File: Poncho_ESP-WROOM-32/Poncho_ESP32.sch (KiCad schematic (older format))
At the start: 20 parts, among them J1 JP_Vcc, J2 JP_TX, J3 JP_RX, J4 CONN_USB2UART, J5 BOOT OPTION, J6 JTAG, U1 LD1117AL-33, U2 ESP32-WROOM

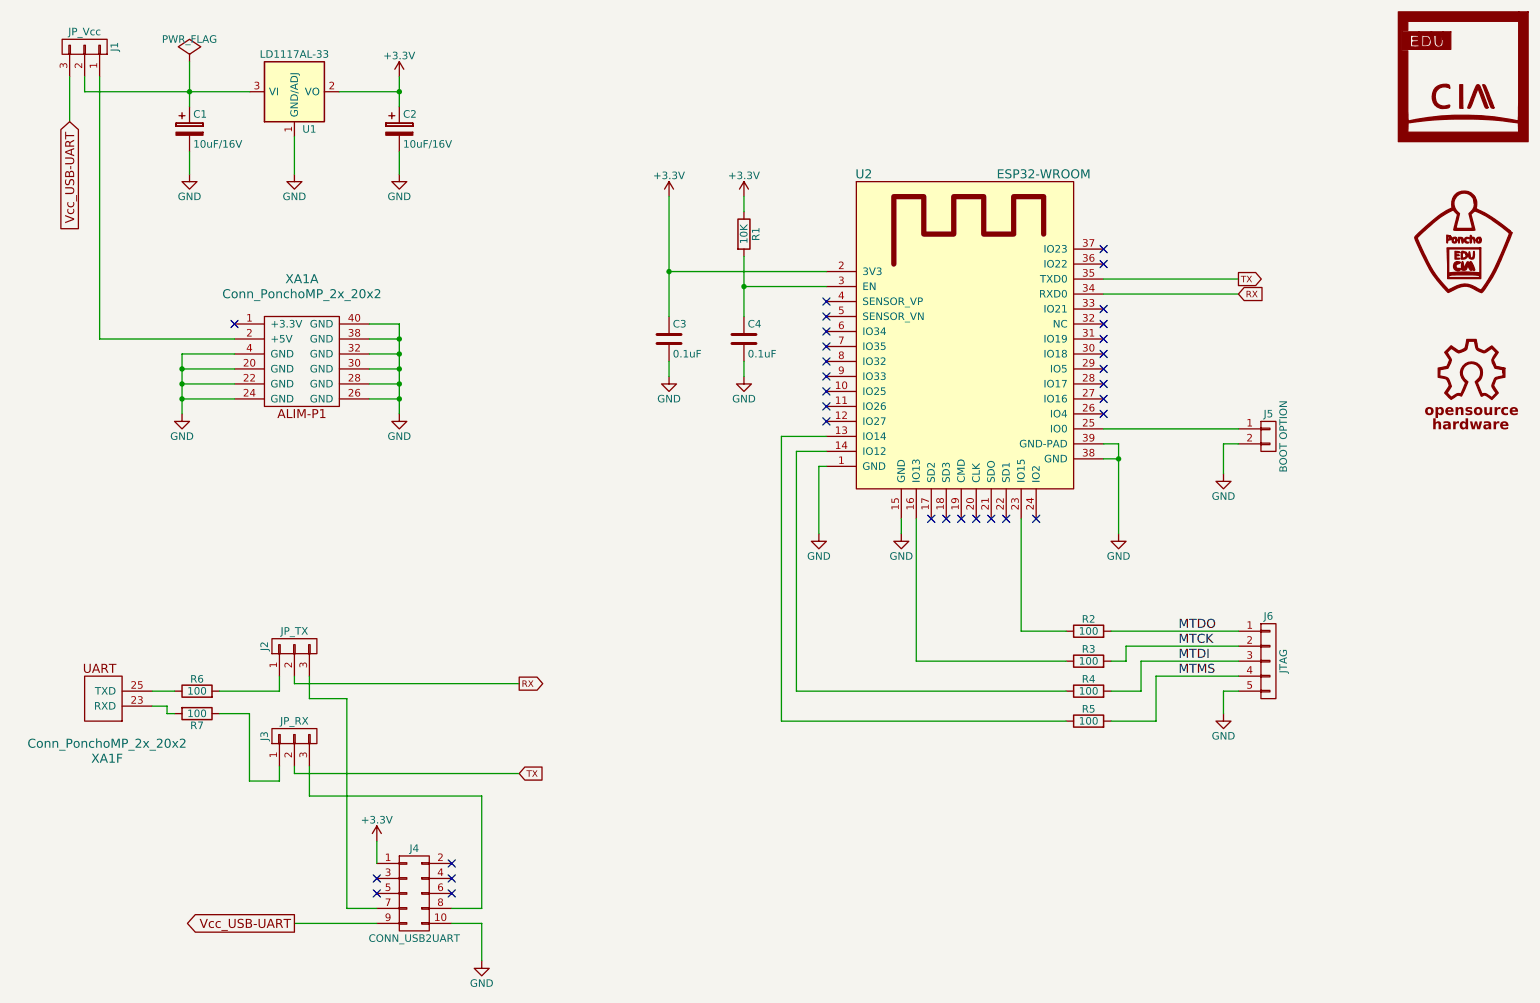
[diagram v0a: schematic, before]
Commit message: Agrego modificaciones enviadas por ivan.s@cika.com  para que el hardware sea compatible con el firmware de comandos AT del módulo.
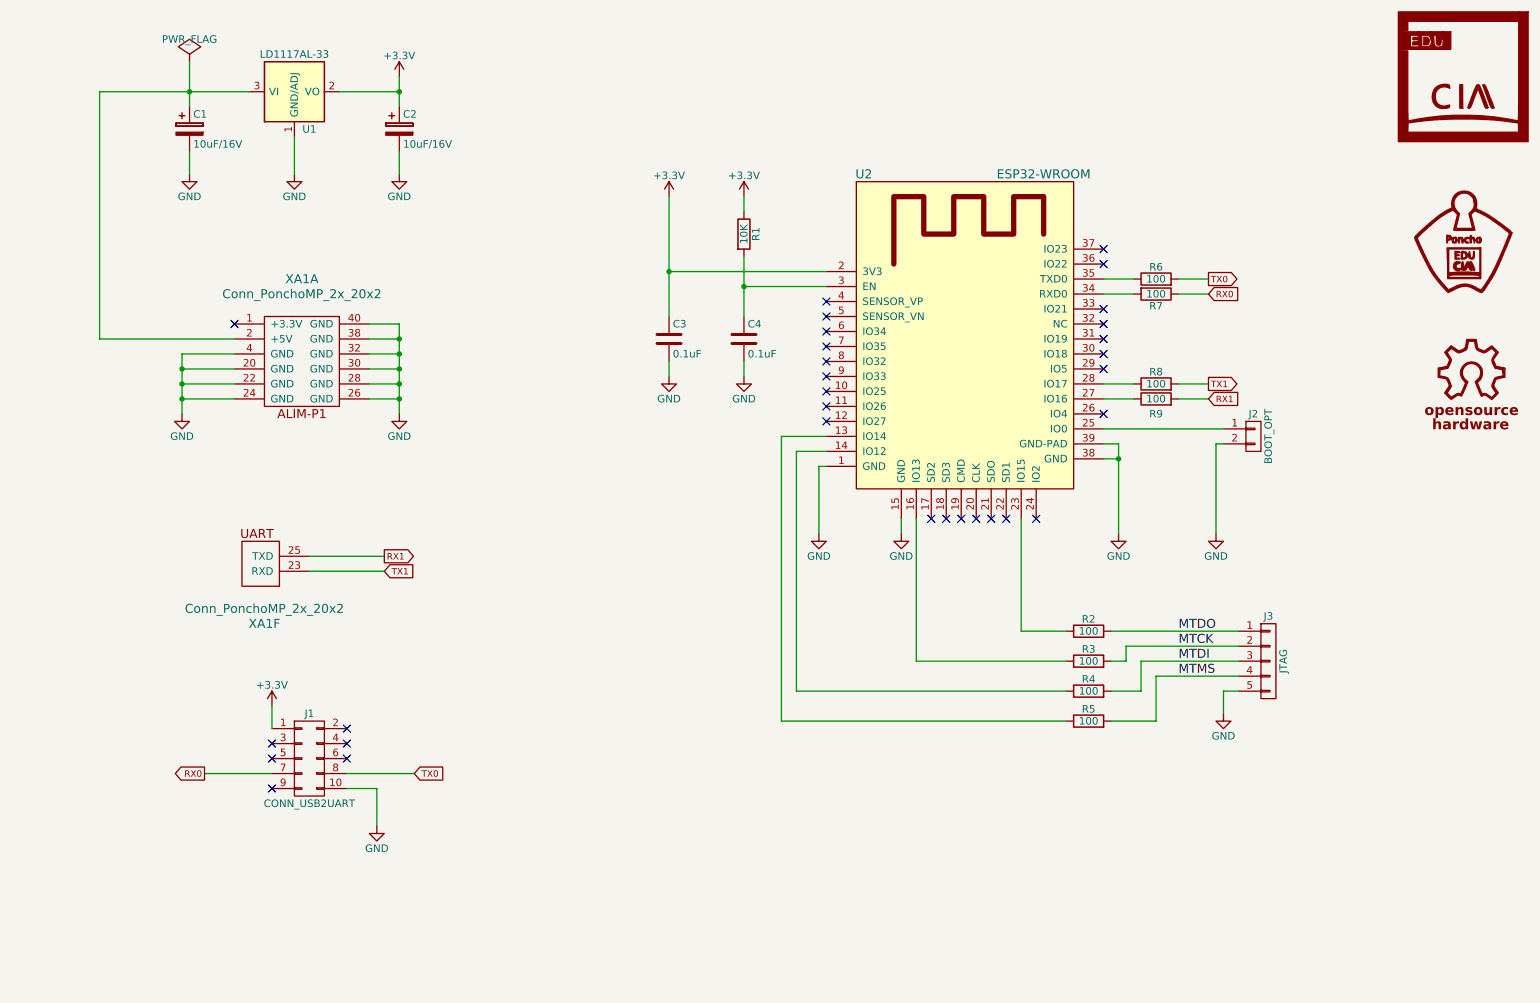
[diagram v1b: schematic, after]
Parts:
- removed J1: JP_Vcc, Pin_Headers:Pin_Header_Straight_1x03_Pitch2.54mm, symbol CONN_01X03
- removed J2: JP_TX, Pin_Headers:Pin_Header_Straight_1x03_Pitch2.54mm, symbol CONN_01X03
- removed J3: JP_RX, Pin_Headers:Pin_Header_Straight_1x03_Pitch2.54mm, symbol CONN_01X03
- removed J5: BOOT OPTION, Pin_Headers:Pin_Header_Straight_1x02_Pitch2.54mm, symbol CONN_01X02
- added J2: BOOT_OPT, Poncho_ESP-WROOM-32:Pin_Header_Straight_1x02_Pitch2.54mm, symbol CONN_01X02
- added R8, R9: 100, Poncho_ESP-WROOM-32:R_0805_HandSoldering, symbol R
- C1, C2: footprint Capacitors_SMD:CP_Elec_4x5.3 -> Poncho_ESP-WROOM-32:CP_Elec_4x5.3
- C3, C4: footprint Capacitors_SMD:C_0805_HandSoldering -> Poncho_ESP-WROOM-32:C_0805_HandSoldering
- J1: renamed from J4; footprint Socket_Strips:Socket_Strip_Angled_2x05_Pitch2.54mm -> Poncho_ESP-WROOM-32:Socket_Strip_Angled_2x05_Pitch2.54mm
- J3: renamed from J6; footprint Pin_Headers:Pin_Header_Straight_1x05_Pitch2.54mm -> Poncho_ESP-WROOM-32:Pin_Header_Straight_1x05_Pitch2.54mm
- R1, R2, R3, R4, R5, R6, R7: footprint Resistors_SMD:R_0805_HandSoldering -> Poncho_ESP-WROOM-32:R_0805_HandSoldering
- U1: footprint TO_SOT_Packages_SMD:SOT-223 -> Poncho_ESP-WROOM-32:SOT-223
- U2: footprint ESP32-footprints-Lib:ESP32-WROOM -> Poncho_ESP-WROOM-32:ESP32-WROOM
- XA1: footprint Poncho_Modelos:Conn_Poncho_Derecha_Sin_Pin_Desc -> Poncho_ESP-WROOM-32:Conn_Poncho_Derecha_Sin_Pin_Desc
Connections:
- net RX is gone; now on an unnamed net: U2.34 (RXD0)
- net TX is gone; now on an unnamed net: U2.35 (TXD0)
- net GND: now also J2.2 (P2)
- net at U2.25 (IO0): now also J2.1 (P1)
- net at U2.27 (IO16): now also R9.1
- net at U2.28 (IO17): now also R8.1
- net at C1.1, U1.3 (VI): now also XA1.2 (+5V)
- net RX0: now reaches J1.7 (P7)
- net RX0: now also R7.1
- net TX0: now reaches J1.8 (P8)
- net TX0: now also R6.2
- net at R7.2: no longer XA1.23 (RXD)
- net at R6.1: no longer XA1.25 (TXD)
- net Vcc_USB-UART: no longer names the net of J1.9 (P9)
- new net RX1: R9.2, XA1.25 (TXD)
- new net TX1: R8.2, XA1.23 (RXD)
- no-connect marks 32 -> 31
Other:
- moved on the sheet: J1, R6, R7, XA1F
